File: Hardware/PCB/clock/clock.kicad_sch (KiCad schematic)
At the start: 65 parts, among them J1 AudioJack2, J2 Synth_power_2x5, J3 AudioJack2, J4 AudioJack2, J5 AudioJack2, J6 AudioJack2, J7 AudioJack2, J8 Conn_02x04_Odd_Even, J9 Conn_02x04_Odd_Even, SW1 RotaryEncoder, SW2 SW_Push, U1 40106

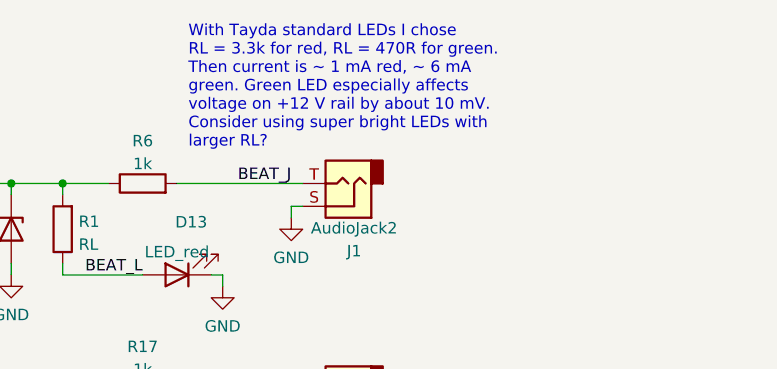
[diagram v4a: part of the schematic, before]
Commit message: AliExpress LEDs and their suitable resistances
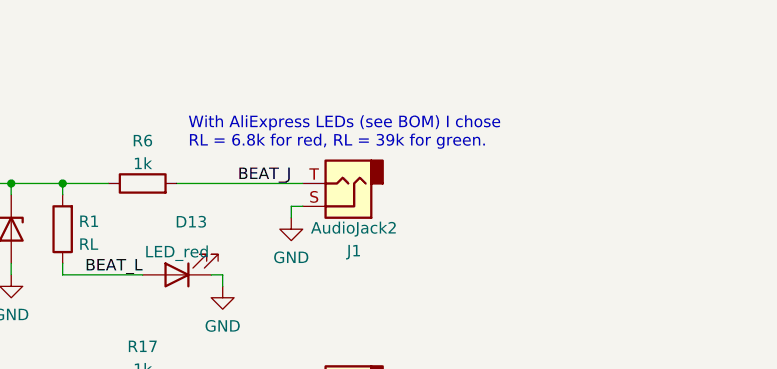
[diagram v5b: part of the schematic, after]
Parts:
- D13: SKU A-1554 -> Fog red LED; Vendor Tayda -> AliExpress YuanQi
- D3, D4, D5, D6, D7: SKU A-1553 -> Fog green LED; Vendor Tayda -> AliExpress YuanQi
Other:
- note added: "With AliExpress LEDs (see BOM) I chose RL = 6.8k for red, RL = 39k for green."
- note removed: "With Tayda standard LEDs I chose RL = 3.3k for red, RL = 470R for green. Then current is ~ 1 mA red, ~ 6 mA green. Green LED especially affects voltage on +12 V rail by about 10 mV. Consider using super bright LEDs with larger RL?"
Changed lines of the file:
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@@
     (effects (font (size 1.27 1.27)) (justify left bottom))
   )
-  (text "With Tayda standard LEDs I chose\nRL = 3.3k for red, RL = 470R for green.\nThen current is ~ 1 mA red, ~ 6 mA\ngreen. Green LED especially affects\nvoltage on +12 V rail by about 10 mV.\nConsider using super bright LEDs with\nlarger RL?"
+  (text "With AliExpress LEDs (see BOM) I chose\nRL = 6.8k for red, RL = 39k for green.\n"
     (at 204.47 27.94 0)
     (effects (font (size 1.27 1.27)) (justify left bottom))
@@
       (effects (font (size 1.27 1.27)) hide)
     )
-    (property "Vendor" "Tayda" (id 4) (at 203.2 64.77 0)
-      (effects (font (size 1.27 1.27)) hide)
-    )
-    (property "SKU" "A-1553" (id 5) (at 203.2 64.77 0)
+    (property "Vendor" "AliExpress YuanQi" (id 4) (at 203.2 64.77 0)
+      (effects (font (size 1.27 1.27)) hide)
+    )
+    (property "SKU" "Fog green LED" (id 5) (at 203.2 64.77 0)
       (effects (font (size 1.27 1.27)) hide)
     )
@@
       (effects (font (size 1.27 1.27)) hide)
     )
-    (property "Vendor" "Tayda" (id 4) (at 203.2 110.49 0)
-      (effects (font (size 1.27 1.27)) hide)
-    )
-    (property "SKU" "A-1553" (id 5) (at 203.2 110.49 0)
+    (property "Vendor" "AliExpress YuanQi" (id 4) (at 203.2 110.49 0)
+      (effects (font (size 1.27 1.27)) hide)
+    )
+    (property "SKU" "Fog green LED" (id 5) (at 203.2 110.49 0)
       (effects (font (size 1.27 1.27)) hide)
     )
@@
       (effects (font (size 1.27 1.27)) hide)
     )
-    (property "Vendor" "Tayda" (id 4) (at 203.2 156.21 0)
-      (effects (font (size 1.27 1.27)) hide)
-    )
-    (property "SKU" "A-1553" (id 5) (at 203.2 156.21 0)
+    (property "Vendor" "AliExpress YuanQi" (id 4) (at 203.2 156.21 0)
+      (effects (font (size 1.27 1.27)) hide)
+    )
+    (property "SKU" "Fog green LED" (id 5) (at 203.2 156.21 0)
       (effects (font (size 1.27 1.27)) hide)
     )
@@
       (effects (font (size 1.27 1.27)) hide)
     )
-    (property "Vendor" "Tayda" (id 4) (at 203.2 133.35 0)
-      (effects (font (size 1.27 1.27)) hide)
-    )
-    (property "SKU" "A-1553" (id 5) (at 203.2 133.35 0)
+    (property "Vendor" "AliExpress YuanQi" (id 4) (at 203.2 133.35 0)
+      (effects (font (size 1.27 1.27)) hide)
+    )
+    (property "SKU" "Fog green LED" (id 5) (at 203.2 133.35 0)
       (effects (font (size 1.27 1.27)) hide)
     )
@@
       (effects (font (size 1.27 1.27)) hide)
     )
-    (property "Vendor" "Tayda" (id 4) (at 203.2 41.91 0)
-      (effects (font (size 1.27 1.27)) hide)
-    )
-    (property "SKU" "A-1554" (id 5) (at 203.2 41.91 0)
+    (property "Vendor" "AliExpress YuanQi" (id 4) (at 203.2 41.91 0)
+      (effects (font (size 1.27 1.27)) hide)
+    )
+    (property "SKU" "Fog red LED" (id 5) (at 203.2 41.91 0)
       (effects (font (size 1.27 1.27)) hide)
     )
@@
       (effects (font (size 1.27 1.27)) hide)
     )
-    (property "Vendor" "Tayda" (id 4) (at 203.2 87.63 0)
-      (effects (font (size 1.27 1.27)) hide)
-    )
-    (property "SKU" "A-1553" (id 5) (at 203.2 87.63 0)
-      (effects (font (size 1.27 1.27)) hide)
-    )
+    (property "Vendor" "AliExpress YuanQi" (id 4) (at 203.2 87.63 0)
+      (effects (font (size 1.27 1.27)) hide)
+    )
+    (property "SKU" "Fog green LED" (id 5) (at 203.2 87.63 0)
+      (effects (font (size 1.27 1.27)) hide)
+    )

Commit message: pre fab updates, gerbers, schem pdf
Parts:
- added B1, B2: Board, ao_tht:Board_Marker, symbol ao_symbols:Board
- D10: renamed from D4; SKU Fog green LED -> A-1553; Vendor AliExpress YuanQi -> Tayda
- D11: renamed from D5; SKU Fog green LED -> A-1553; Vendor AliExpress YuanQi -> Tayda
- D12: renamed from D6; SKU Fog green LED -> A-1553; Vendor AliExpress YuanQi -> Tayda
- D13: renamed from D7; SKU Fog green LED -> A-1553; Vendor AliExpress YuanQi -> Tayda
- D8: renamed from D13; SKU Fog red LED -> A-1554; Vendor AliExpress YuanQi -> Tayda
- D9: renamed from D3; SKU Fog green LED -> A-1553; Vendor AliExpress YuanQi -> Tayda
- renumbered C4 to C1, C1 to C2, C2 to C3, C3 to C4, D2 to D1, D1 to D2, D8 to D3, D9 to D4, D10 to D5, D11 to D6, D12 to D7, H3 to H2, H2 to H3, J9 to J1, J8 to J3, J1 to J4, J3 to J5, J4 to J6, J5 to J7, J6 to J8, J7 to J9, R5 to R1, R12 to R10, R13 to R11, R14 to R12, R15 to R13, R16 to R14, R6 to R15, R17 to R16, R18 to R17, R19 to R18, R20 to R19, R10 to R2, R21 to R20, R2 to R3, R3 to R4, R4 to R5, R7 to R6, R8 to R7, R9 to R8, R1 to R9, SW2 to SW1, SW1 to SW2
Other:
- note added: "CONTROLS BOARD"
